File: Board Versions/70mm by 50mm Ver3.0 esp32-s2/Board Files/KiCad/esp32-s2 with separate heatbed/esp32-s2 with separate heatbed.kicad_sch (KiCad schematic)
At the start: 46 parts, among them IC1 ESP32-S2FN4R2, J1 PJ-037B, J2 USB4520-03-0-A, U1 LD1117S33TR_SOT223, U2 MAX31855KASA, Y1 ECS-400-15-33B-CTN-TR

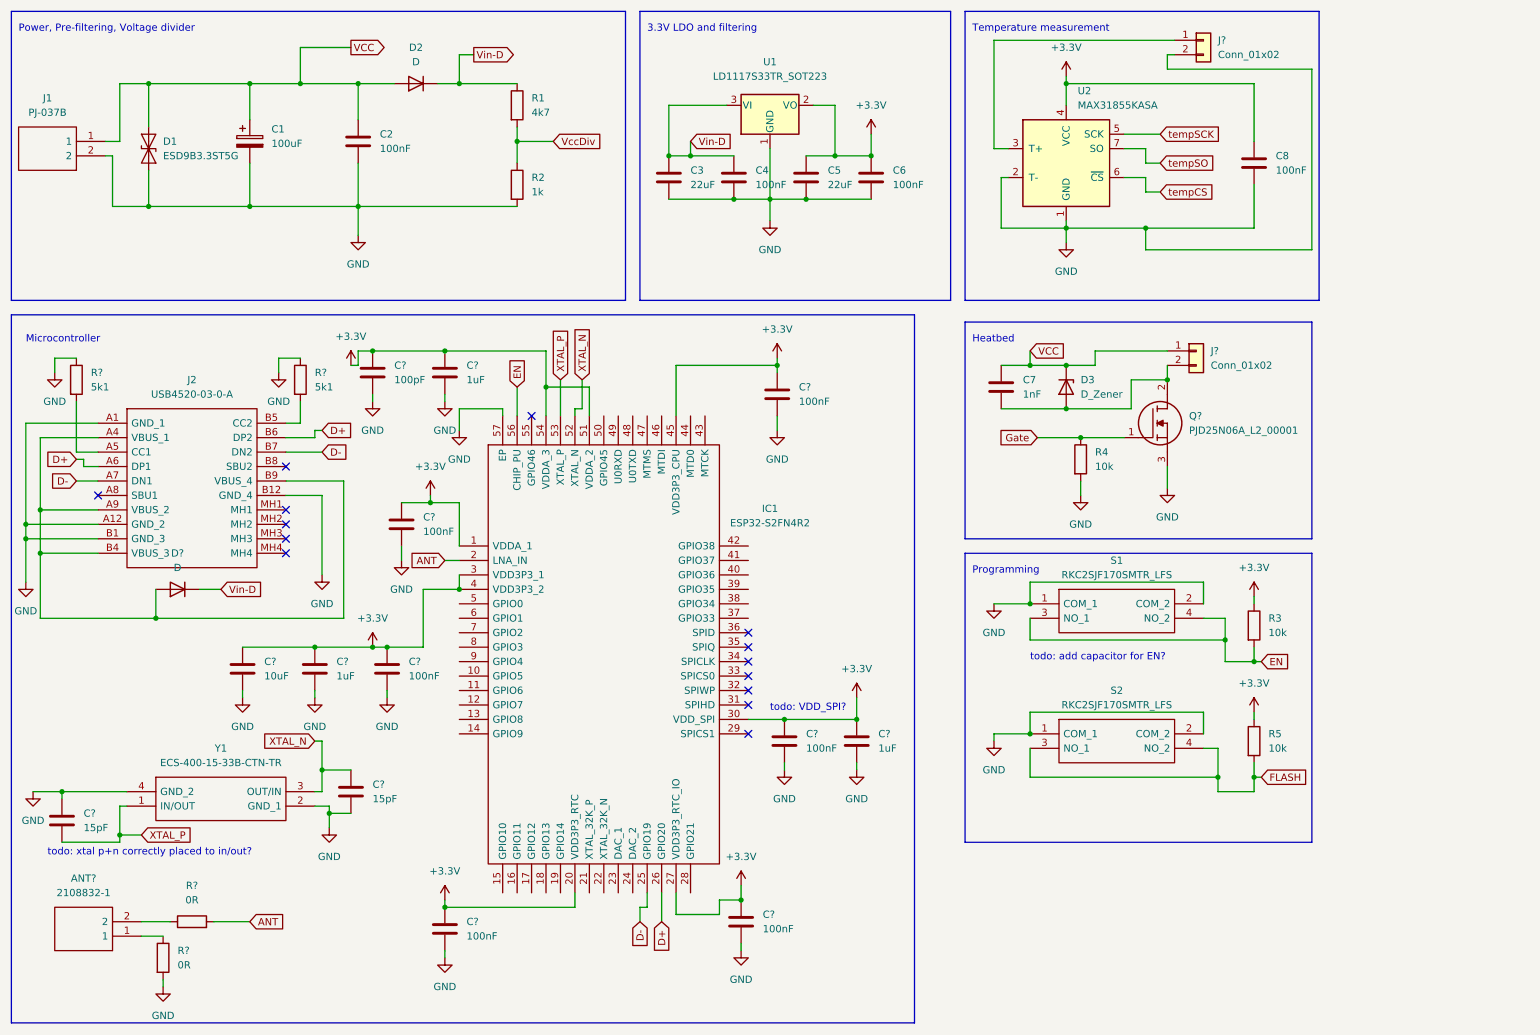
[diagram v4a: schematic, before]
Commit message: Vdd SPI no 3.3V, and add capacitor for EN
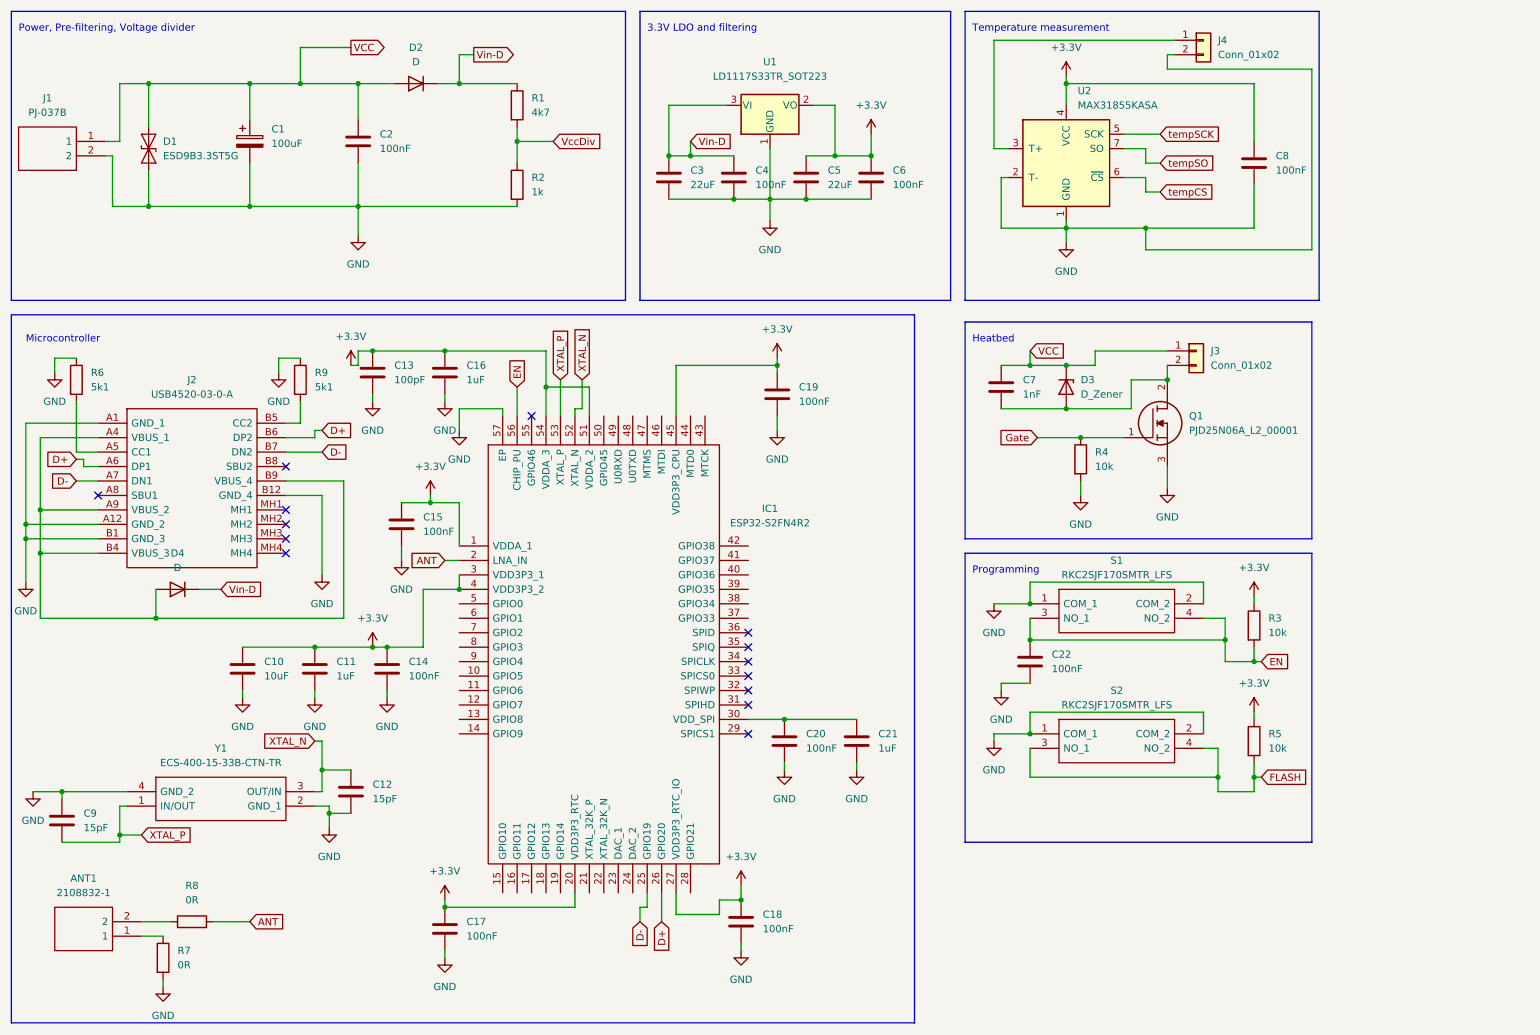
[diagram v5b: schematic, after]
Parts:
- added C22: 100nF, Capacitor_SMD:C_0603_1608Metric, symbol Device:C
- ANT1: renamed from ANT?; footprint 21088321 -> library_manager:21088321
- IC1: footprint QFN40P700X700X90-57N-D -> library_manager:QFN40P700X700X90-57N-D
- J1: footprint PJ037B -> library_manager:PJ037B
- J2: footprint USB4520030A -> library_manager:USB4520030A
- Q1: renamed from Q?; footprint PJD25N06A_L2_00001 -> library_manager:PJD25N06A_L2_00001
- S1, S2: footprint RKC2SJF170SMTRLFS -> library_manager:RKC2SJF170SMTRLFS
- Y1: footprint ECS2501033BCKMTR -> library_manager:ECS2501033BCKMTR
- gave numbers to parts that had none: 20
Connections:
- net +3V3: no longer C20.1, C21.1, IC1.30 (VDD_SPI)
- net EN: now also C22.1
- net GND: now also C22.2
- new net: C20.1, C21.1, IC1.30 (VDD_SPI)
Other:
- note removed: "todo: VDD_SPI?"
- note removed: "todo: add capacitor for EN?"
- note removed: "todo: xtal p+n correctly placed to in/out?"

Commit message: Footprints and connect  esp32 peripherals
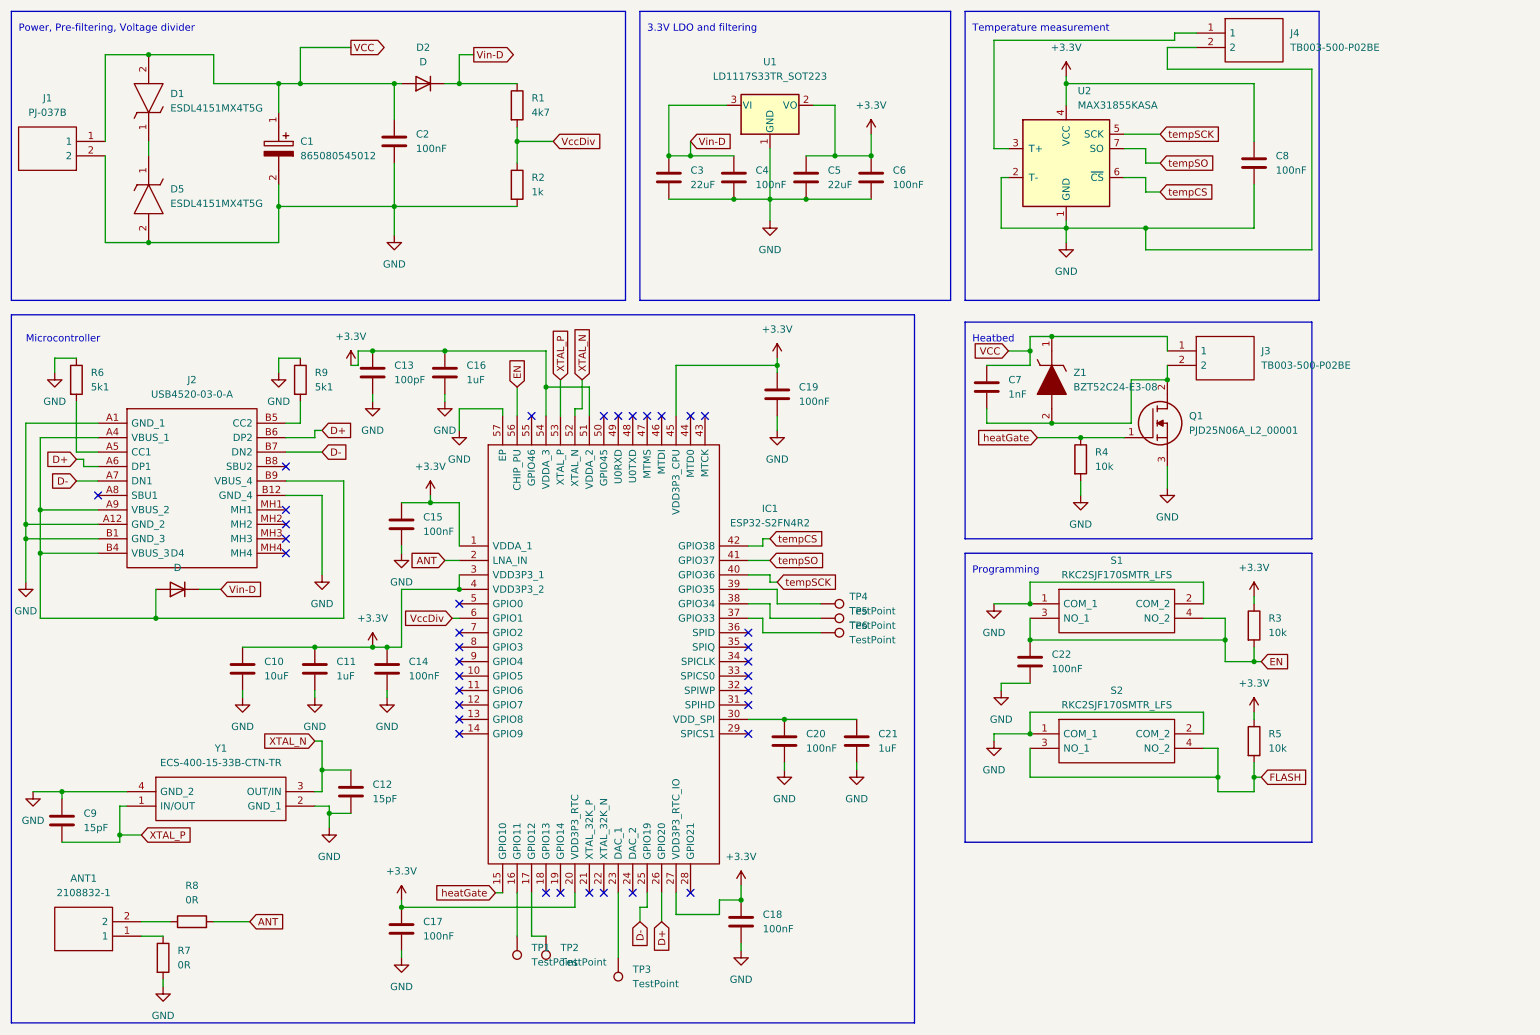
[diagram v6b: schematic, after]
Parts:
- removed C1: 100uF, symbol Device:C_Polarized
- removed D1: ESD9B3.3ST5G, Diode_SMD:D_SOD-923, symbol Diode:ESD9B3.3ST5G
- removed D3: D_Zener, symbol Device:D_Zener
- removed J3, J4: Conn_01x02, symbol Connector_Generic:Conn_01x02
- added C1: 865080545012, library_manager:CAPAE660X770N, symbol library_loader:865080545012
- added D1, D5: ESDL4151MX4T5G, library_manager:ESDL4151MX4T5G, symbol library_loader:ESDL4151MX4T5G
- added J3, J4: TB003-500-P02BE, library_manager:SHDR2W100P0X500_1X2_1000X780X1030P, symbol library_loader:TB003-500-P02BE
- added TP1, TP2, TP3, TP4, TP5, TP6: TestPoint, Connector_PinHeader_2.54mm:PinHeader_1x01_P2.54mm_Vertical, symbol Connector:TestPoint
- added Z1: BZT52C24-E3-08, library_manager:BZT52C24E308, symbol library_loader:BZT52C24-E3-08
- C10, C11, C12, C13, C14, C15, C16, C17, C18, C19, C2, C20, C21, C3, C4, C5, C6, C7, C8, C9: footprint (none) -> Capacitor_SMD:C_0603_1608Metric
- D2, D4: footprint (none) -> Diode_SMD:D_SOD-123
- R1, R2, R3, R4, R5, R6, R7, R8, R9: footprint (none) -> Resistor_SMD:R_0603_1608Metric
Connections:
- net Gate is gone; now on net heatGate: Q1.1, R4.1
- net GND: now also C1.2, D5.2, J4.2
- net VCC: now also C1.1, D1.2, J3.1, Z1.1
- net VccDiv: now also IC1.6 (GPIO1)
- net tempCS: now also IC1.42 (GPIO38)
- net tempSCK: now also IC1.40 (GPIO36)
- net tempSO: now also IC1.41 (GPIO37)
- net at U2.3 (T+): now also J4.1
- net at C7.2, Q1.2: now also J3.2, Z1.2
- net heatGate: now reaches IC1.15 (GPIO10)
- net at IC1.16 (GPIO11): now also TP1.1
- net at IC1.17 (GPIO12): now also TP2.1
- net at IC1.23 (DAC_1): now also TP3.1
- net at IC1.37 (GPIO33): now also TP6.1
- net at IC1.38 (GPIO34): now also TP5.1
- net at IC1.39 (GPIO35): now also TP4.1
- new net: D1.1, D5.1
- no-connect marks 14 -> 36
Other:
- moved on the sheet: C17, C2, C7, D2

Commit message: Add leds (and other things I don't remember)
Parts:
- added D3, D6: LED, Diode_SMD:D_0603_1608Metric, symbol Device:LED
- added R10: 10k, Resistor_SMD:R_0603_1608Metric, symbol Device:R
- added R11, R12: 2k, Resistor_SMD:R_0603_1608Metric, symbol Device:R
- C3, C5, C7: footprint Capacitor_SMD:C_0603_1608Metric -> Capacitor_SMD:C_0805_2012Metric
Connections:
- net +3V3: now also R10.1
- net FLASH: now also IC1.5 (GPIO0)
- net GND: now also D3.1 (K), D6.1 (K)
- net led1: now reaches IC1.13 (GPIO8)
- net led1: now also R11.1
- net led2: now reaches IC1.14 (GPIO9)
- net led2: now also R12.1
- net at IC1.24 (DAC_2): now also R10.2
- new net: D3.2 (A), R12.2
- new net: D6.2 (A), R11.2
- no-connect marks 36 -> 32
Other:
- note added: "leds"
- moved on the sheet: C18

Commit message: Routing complete
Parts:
- removed TP1, TP2, TP3, TP4, TP5, TP6: TestPoint, Connector_PinHeader_2.54mm:PinHeader_1x01_P2.54mm_Vertical, symbol Connector:TestPoint
- added J5: Conn_01x03_Male, Connector_PinHeader_2.54mm:PinHeader_1x03_P2.54mm_Vertical, symbol Connector:Conn_01x03_Male
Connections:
- net at IC1.39 (GPIO35): now also J5.3 (Pin_3)
- net at IC1.37 (GPIO33): now also J5.1 (Pin_1)
- net at IC1.38 (GPIO34): now also J5.2 (Pin_2)
- no-connect marks 32 -> 35
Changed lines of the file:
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@@
   (no_connect (at 95.25 134.62))
   (no_connect (at 95.25 137.16))
-  (no_connect (at 113.03 170.18))
   (no_connect (at 110.49 170.18))
+  (no_connect (at 113.03 170.18))
+  (no_connect (at 123.19 170.18))
+  (no_connect (at 107.95 170.18))
+  (no_connect (at 105.41 170.18))
   (no_connect (at 146.05 124.46))
   (no_connect (at 146.05 127))
@@
     (stroke (width 0) (type default) (color 0 0 0 0))
   )
-  (wire (pts (xy 123.19 170.18) (xy 123.19 181.61))
-    (stroke (width 0) (type default) (color 0 0 0 0))
-  )
   (wire (pts (xy 21.59 90.17) (xy 21.59 102.87))
     (stroke (width 0) (type default) (color 0 0 0 0))
@@
     (stroke (width 0) (type default) (color 0 0 0 0))
   )
-  (wire (pts (xy 105.41 170.18) (xy 105.41 177.8))
-    (stroke (width 0) (type default) (color 0 0 0 0))
-  )
   (wire (pts (xy 25.4 161.29) (xy 35.56 161.29))
     (stroke (width 0) (type default) (color 0 0 0 0))
@@
     (stroke (width 0) (type default) (color 0 0 0 0))
   )
-  (wire (pts (xy 107.95 177.8) (xy 107.95 170.18))
-    (stroke (width 0) (type default) (color 0 0 0 0))
-  )
   (wire (pts (xy 67.31 21.59) (xy 67.31 27.94))
     (stroke (width 0) (type default) (color 0 0 0 0))
@@
     (stroke (width 0) (type default) (color 0 0 0 0))
   )
-  (wire (pts (xy 110.49 177.8) (xy 107.95 177.8))
-    (stroke (width 0) (type default) (color 0 0 0 0))
-  )
   (wire (pts (xy 132.08 40.64) (xy 135.89 40.64))
     (stroke (width 0) (type default) (color 0 0 0 0))
@@
     (pin "1")
   )
-  (symbol (lib_id "Connector:TestPoint") (at 105.41 177.8 180) (unit 1)
-    (in_bom yes) (on_board yes) (fields_autoplaced)
-    (property "Reference" "TP1" (id 0) (at 107.95 179.8319 0)
-      (effects (font (size 1.27 1.27)) (justify right))
-    )
-    (property "Value" "TestPoint" (id 1) (at 107.95 182.3719 0)
-      (effects (font (size 1.27 1.27)) (justify right))
-    )
-    (property "Footprint" "Connector_PinHeader_2.54mm:PinHeader_1x01_P2.54mm_Vertical" (id 2) (at 100.33 177.8 0)
-      (effects (font (size 1.27 1.27)) hide)
-    )
-    (property "Datasheet" "~" (id 3) (at 100.33 177.8 0)
-      (effects (font (size 1.27 1.27)) hide)
-    )
-    (pin "1")
-  )
   (symbol (lib_id "Device:R") (at 260.35 144.78 0) (unit 1)
     (in_bom yes) (on_board yes) (fields_autoplaced)
@@
     (pin "2")
   )
-  (symbol (lib_id "Connector:TestPoint") (at 158.75 119.38 270) (unit 1)
-    (in_bom yes) (on_board yes) (fields_autoplaced)
-    (property "Reference" "TP4" (id 0) (at 163.83 118.1099 90)
-      (effects (font (size 1.27 1.27)) (justify left))
-    )
-    (property "Value" "TestPoint" (id 1) (at 163.83 120.6499 90)
-      (effects (font (size 1.27 1.27)) (justify left))
-    )
-    (property "Footprint" "Connector_PinHeader_2.54mm:PinHeader_1x01_P2.54mm_Vertical" (id 2) (at 158.75 124.46 0)
-      (effects (font (size 1.27 1.27)) hide)
-    )
-    (property "Datasheet" "~" (id 3) (at 158.75 124.46 0)
-      (effects (font (size 1.27 1.27)) hide)
-    )
-    (pin "1")
-  )
   (symbol (lib_id "power:+3.3V") (at 167.64 36.83 0) (unit 1)
     (in_bom yes) (on_board yes) (fields_autoplaced)
@@
     (pin "2")
   )
-  (symbol (lib_id "Connector:TestPoint") (at 110.49 177.8 180) (unit 1)
-    (in_bom yes) (on_board yes) (fields_autoplaced)
-    (property "Reference" "TP2" (id 0) (at 113.03 179.8319 0)
-      (effects (font (size 1.27 1.27)) (justify right))
-    )
-    (property "Value" "TestPoint" (id 1) (at 113.03 182.3719 0)
-      (effects (font (size 1.27 1.27)) (justify right))
-    )
-    (property "Footprint" "Connector_PinHeader_2.54mm:PinHeader_1x01_P2.54mm_Vertical" (id 2) (at 105.41 177.8 0)
-      (effects (font (size 1.27 1.27)) hide)
-    )
-    (property "Datasheet" "~" (id 3) (at 105.41 177.8 0)
-      (effects (font (size 1.27 1.27)) hide)
-    )
-    (pin "1")
-  )
   (symbol (lib_id "Device:C") (at 83.82 38.1 0) (unit 1)
     (in_bom yes) (on_board yes) (fields_autoplaced)
@@
     (pin "1")
   )
-  (symbol (lib_id "Connector:TestPoint") (at 158.75 124.46 270) (unit 1)
-    (in_bom yes) (on_board yes) (fields_autoplaced)
-    (property "Reference" "TP6" (id 0) (at 163.83 123.1899 90)
-      (effects (font (size 1.27 1.27)) (justify left))
-    )
-    (property "Value" "TestPoint" (id 1) (at 163.83 125.7299 90)
-      (effects (font (size 1.27 1.27)) (justify left))
-    )
-    (property "Footprint" "Connector_PinHeader_2.54mm:PinHeader_1x01_P2.54mm_Vertical" (id 2) (at 158.75 129.54 0)
-      (effects (font (size 1.27 1.27)) hide)
-    )
-    (property "Datasheet" "~" (id 3) (at 158.75 129.54 0)
-      (effects (font (size 1.27 1.27)) hide)
-    )
-    (pin "1")
-  )
   (symbol (lib_id "library_loader:PJ-037B") (at 33.02 40.64 180) (unit 1)
     (in_bom yes) (on_board yes) (fields_autoplaced)
@@
     (pin "1")
   )
-  (symbol (lib_id "Connector:TestPoint") (at 158.75 121.92 270) (unit 1)
-    (in_bom yes) (on_board yes) (fields_autoplaced)
-    (property "Reference" "TP5" (id 0) (at 163.83 120.6499 90)
-      (effects (font (size 1.27 1.27)) (justify left))
-    )
-    (property "Value" "TestPoint" (id 1) (at 163.83 123.1899 90)
-      (effects (font (size 1.27 1.27)) (justify left))
-    )
-    (property "Footprint" "Connector_PinHeader_2.54mm:PinHeader_1x01_P2.54mm_Vertical" (id 2) (at 158.75 127 0)
-      (effects (font (size 1.27 1.27)) hide)
-    )
-    (property "Datasheet" "~" (id 3) (at 158.75 127 0)
-      (effects (font (size 1.27 1.27)) hide)
-    )
-    (pin "1")
-  )
   (symbol (lib_id "Device:R") (at 27.94 80.01 0) (unit 1)
     (in_bom yes) (on_board yes) (fields_autoplaced)
@@
     (pin "1")
   )
+  (symbol (lib_id "Connector:Conn_01x03_Male") (at 163.83 121.92 180) (unit 1)
+    (in_bom yes) (on_board yes) (fields_autoplaced)
+    (property "Reference" "J5" (id 0) (at 165.1 120.6499 0)
+      (effects (font (size 1.27 1.27)) (justify right))
+    )
+    (property "Value" "Conn_01x03_Male" (id 1) (at 165.1 123.1899 0)
+      (effects (font (size 1.27 1.27)) (justify right))
+    )
+    (property "Footprint" "Connector_PinHeader_2.54mm:PinHeader_1x03_P2.54mm_Vertical" (id 2) (at 163.83 121.92 0)
+      (effects (font (size 1.27 1.27)) hide)
+    )
+    (property "Datasheet" "~" (id 3) (at 163.83 121.92 0)
+      (effects (font (size 1.27 1.27)) hide)
+    )
+    (pin "1")
+    (pin "2")
+    (pin "3")
+  )
   (symbol (lib_id "power:GND") (at 92.71 83.82 0) (unit 1)
     (in_bom yes) (on_board yes) (fields_autoplaced)
@@
     (pin "1")
   )
-  (symbol (lib_id "Connector:TestPoint") (at 123.19 181.61 180) (unit 1)
-    (in_bom yes) (on_board yes) (fields_autoplaced)
-    (property "Reference" "TP3" (id 0) (at 125.73 183.6419 0)
-      (effects (font (size 1.27 1.27)) (justify right))
-    )
-    (property "Value" "TestPoint" (id 1) (at 125.73 186.1819 0)
-      (effects (font (size 1.27 1.27)) (justify right))
-    )
-    (property "Footprint" "Connector_PinHeader_2.54mm:PinHeader_1x01_P2.54mm_Vertical" (id 2) (at 118.11 181.61 0)
-      (effects (font (size 1.27 1.27)) hide)
-    )
-    (property "Datasheet" "~" (id 3) (at 118.11 181.61 0)
-      (effects (font (size 1.27 1.27)) hide)
-    )
-    (pin "1")
-  )
   (symbol (lib_id "power:GND") (at 24.13 78.74 0) (unit 1)
     (in_bom yes) (on_board yes) (fields_autoplaced)
@@
       (reference "J4") (unit 1) (value "TB003-500-P02BE") (footprint "library_manager:SHDR2W100P0X500_1X2_1000X780X1030P")
     )
+    (path "/ad6cfbb5-6560-4e8d-b51f-2fc576abbdaf"
+      (reference "J5") (unit 1) (value "Conn_01x03_Male") (footprint "Connector_PinHeader_2.54mm:PinHeader_1x03_P2.54mm_Vertical")
+    )
     (path "/4cebe0d3-dd69-4a3c-8afb-1f7ed5f46b3f"
       (reference "Q1") (unit 1) (value "PJD25N06A_L2_00001") (footprint "library_manager:PJD25N06A_L2_00001")
@@
       (reference "S2") (unit 1) (value "RKC2SJF170SMTR_LFS") (footprint "library_manager:RKC2SJF170SMTRLFS")
     )
-    (path "/11193139-e627-47b8-acb2-c7465a48e18b"
-      (reference "TP1") (unit 1) (value "TestPoint") (footprint "Connector_PinHeader_2.54mm:PinHeader_1x01_P2.54mm_Vertical")
-    )
-    (path "/4967b1ed-cf9b-4db7-9bd1-e8a2d70f4a53"
-      (reference "TP2") (unit 1) (value "TestPoint") (footprint "Connector_PinHeader_2.54mm:PinHeader_1x01_P2.54mm_Vertical")
-    )
-    (path "/e1996bfa-6f33-4144-b3b8-0ecaa63a9bf1"
-      (reference "TP3") (unit 1) (value "TestPoint") (footprint "Connector_PinHeader_2.54mm:PinHeader_1x01_P2.54mm_Vertical")
-    )
-    (path "/3806a371-9c6c-48e3-8acc-c75ec9bc196b"
-      (reference "TP4") (unit 1) (value "TestPoint") (footprint "Connector_PinHeader_2.54mm:PinHeader_1x01_P2.54mm_Vertical")
-    )
-    (path "/929d007f-ac7c-4a9f-b46d-d6c7bd0e649e"
-      (reference "TP5") (unit 1) (value "TestPoint") (footprint "Connector_PinHeader_2.54mm:PinHeader_1x01_P2.54mm_Vertical")
-    )
-    (path "/8c3d3de0-d23f-45b0-b638-d3824cb5c779"
-      (reference "TP6") (unit 1) (value "TestPoint") (footprint "Connector_PinHeader_2.54mm:PinHeader_1x01_P2.54mm_Vertical")
-    )
     (path "/db94c8fc-a32f-4093-9a65-a86b21b63695"
